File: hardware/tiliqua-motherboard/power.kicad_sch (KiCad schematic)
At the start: 32 parts, among them J6 CONN 2x5 P=2.54mm, U10 TPS7A91, U5 AP63200WU

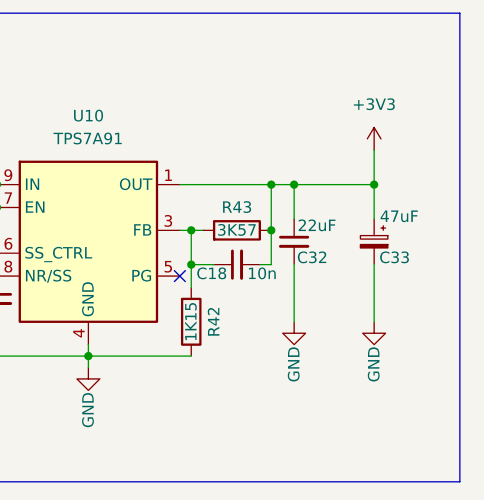
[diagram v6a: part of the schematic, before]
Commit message: hw/mobo-r3: 2nd electrolytic, OSHW on top, layout cleanup
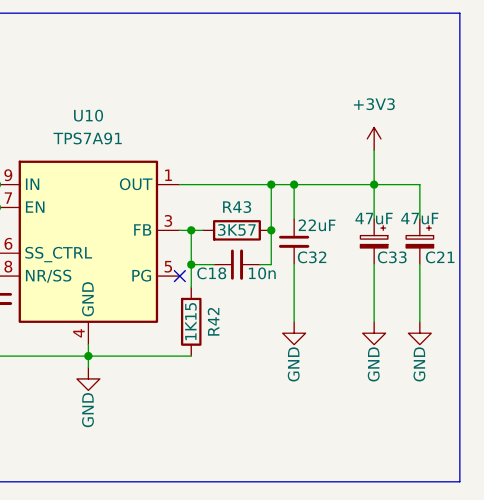
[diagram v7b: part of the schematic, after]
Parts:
- added C21: 47uF, Capacitor_SMD:CP_Elec_6.3x5.4, symbol Device:C_Polarized_Small
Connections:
- net +3V3: now also C21.1
- net GND: now also C21.2
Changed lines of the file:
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@@
 	(wire
 		(pts
+			(xy 274.32 118.11) (xy 274.32 114.3)
+		)
+		(stroke
+			(width 0)
+			(type default)
+		)
+	)
+	(wire
+		(pts
 			(xy 50.8 111.76) (xy 58.42 111.76)
 		)
@@
 	(wire
 		(pts
+			(xy 274.32 123.19) (xy 274.32 129.54)
+		)
+		(stroke
+			(width 0)
+			(type default)
+		)
+	)
+	(wire
+		(pts
 			(xy 237.49 133.35) (xy 237.49 132.08)
 		)
@@
 	(wire
 		(pts
+			(xy 274.32 114.3) (xy 269.24 114.3)
+		)
+		(stroke
+			(width 0)
+			(type default)
+		)
+	)
+	(wire
+		(pts
 			(xy 139.7 123.19) (xy 139.7 129.54)
 		)
@@
 	)
 	(symbol
+		(lib_id "power:GND")
+		(at 274.32 129.54 0)
+		(mirror y)
+		(unit 1)
+		(exclude_from_sim no)
+		(in_bom yes)
+		(on_board yes)
+		(dnp no)
+		(property "Reference" "#PWR012"
+			(at 274.32 135.89 0)
+			(effects
+				(font
+					(size 1.27 1.27)
+				)
+				(hide yes)
+			)
+		)
+		(property "Value" "GND"
+			(at 274.32 136.271 90)
+			(effects
+				(font
+					(size 1.27 1.27)
+				)
+				(justify left)
+			)
+		)
+		(property "Footprint" ""
+			(at 274.32 129.54 0)
+			(effects
+				(font
+					(size 1.27 1.27)
+				)
+				(hide yes)
+			)
+		)
+		(property "Datasheet" ""
+			(at 274.32 129.54 0)
+			(effects
+				(font
+					(size 1.27 1.27)
+				)
+				(hide yes)
+			)
+		)
+		(property "Description" ""
+			(at 274.32 129.54 0)
+			(effects
+				(font
+					(size 1.27 1.27)
+				)
+				(hide yes)
+			)
+		)
+		(pin "1"
+		)
+		(instances
+			(project "tiliqua-motherboard"
+				(path "/df6062c3-a570-4505-924c-c7fe32df3670/4885642e-e1b2-4a9c-a477-910295b2621e"
+					(reference "#PWR012")
+					(unit 1)
+				)
+			)
+		)
+	)
+	(symbol
 		(lib_id "Device:L_Ferrite_Small")
 		(at 77.47 57.15 90)
@@
 	)
 	(symbol
+		(lib_id "Device:C_Polarized_Small")
+		(at 274.32 120.65 0)
+		(mirror y)
+		(unit 1)
+		(exclude_from_sim no)
+		(in_bom yes)
+		(on_board yes)
+		(dnp no)
+		(property "Reference" "C21"
+			(at 276.606 122.428 0)
+			(effects
+				(font
+					(size 1.27 1.27)
+				)
+			)
+		)
+		(property "Value" "47uF"
+			(at 274.32 118.11 0)
+			(effects
+				(font
+					(size 1.27 1.27)
+				)
+			)
+		)
+		(property "Footprint" "Capacitor_SMD:CP_Elec_6.3x5.4"
+			(at 274.32 120.65 0)
+			(effects
+				(font
+					(size 1.27 1.27)
+				)
+				(hide yes)
+			)
+		)
+		(property "Datasheet" "https://datasheet.lcsc.com/lcsc/1809050343_Rubycon-25SEV47M6-3X5-5_C88735.pdf"
+			(at 274.32 120.65 0)
+			(effects
+				(font
+					(size 1.27 1.27)
+				)
+				(hide yes)
+			)
+		)
+		(property "Description" ""
+			(at 274.32 120.65 0)
+			(effects
+				(font
+					(size 1.27 1.27)
+				)
+				(hide yes)
+			)
+		)
+		(property "dig#" ""
+			(at 271.78 128.27 0)
+			(effects
+				(font
+					(size 1.27 1.27)
+				)
+				(hide yes)
+			)
+		)
+		(property "mfg#" "25SEV47M6.3X5.5"
+			(at 271.78 130.81 0)
+			(effects
+				(font
+					(size 1.27 1.27)
+				)
+				(hide yes)
+			)
+		)
+		(property "lcsc#" "C88735"
+			(at 274.32 120.65 0)
+			(effects
+				(font
+					(size 1.27 1.27)
+				)
+				(hide yes)
+			)
+		)
+		(property "Tol" ""
+			(at 274.32 120.65 0)
+			(effects
+				(font
+					(size 1.27 1.27)
+				)
+				(hide yes)
+			)
+		)
+		(pin "1"
+		)
+		(pin "2"
+		)
+		(instances
+			(project "tiliqua-motherboard"
+				(path "/df6062c3-a570-4505-924c-c7fe32df3670/4885642e-e1b2-4a9c-a477-910295b2621e"
+					(reference "C21")
+					(unit 1)
+				)
+			)
+		)
+	)
+	(symbol
 		(lib_id "Diode:US1G")
 		(at 66.04 58.42 0)
@@
 		(dnp no)
 		(property "Reference" "C33"
-			(at 271.526 122.428 0)
+			(at 271.272 122.428 0)
 			(effects
 				(font
@@
 		)
 		(property "Value" "47uF"
-			(at 272.034 117.856 0)
+			(at 269.24 118.11 0)
 			(effects
 				(font

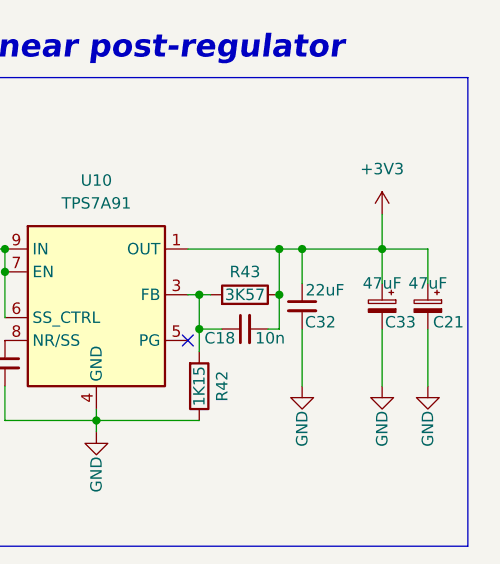
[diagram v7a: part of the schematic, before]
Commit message: hw/mobo-r3: assign remaining part numbers
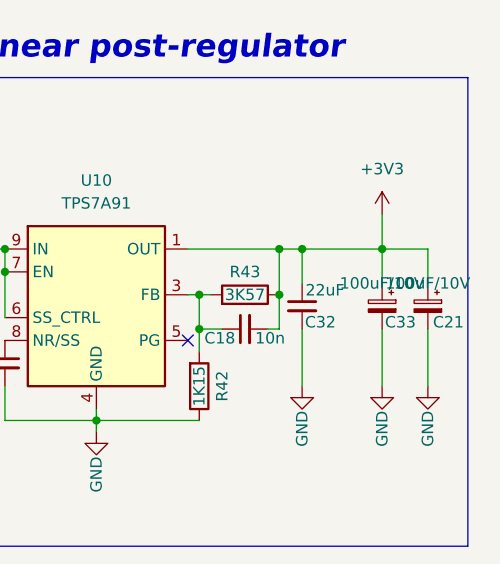
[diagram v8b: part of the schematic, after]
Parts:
- C17, C25, C28, C30: lcsc# (none) -> C131394
- C21, C33: value 47uF -> 100uF/10V; lcsc# C88735 -> C88795
- C31: lcsc# (none) -> C77177
- R42: lcsc# (none) -> C29401
- R43: lcsc# (none) -> C270609
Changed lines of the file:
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@@
 			)
 		)
-		(property "lcsc#" ""
+		(property "lcsc#" "C131394"
 			(at 50.8 115.57 0)
 			(effects
@@
 			)
 		)
-		(property "Value" "47uF"
+		(property "Value" "100uF/10V"
 			(at 274.32 118.11 0)
 			(effects
@@
 			)
 		)
-		(property "lcsc#" "C88735"
+		(property "lcsc#" "C88795"
 			(at 274.32 120.65 0)
 			(effects
@@
 			)
 		)
-		(property "lcsc#" ""
+		(property "lcsc#" "C131394"
 			(at 227.33 127 0)
 			(effects
@@
 			)
 		)
-		(property "lcsc#" ""
+		(property "lcsc#" "C131394"
 			(at 215.9 120.65 0)
 			(effects
@@
 			)
 		)
-		(property "lcsc#" ""
+		(property "lcsc#" "C131394"
 			(at 88.9 114.3 0)
 			(effects
@@
 			)
 		)
-		(property "Value" "47uF"
+		(property "Value" "100uF/10V"
 			(at 269.24 118.11 0)
 			(effects
@@
 			)
 		)
-		(property "lcsc#" "C88735"
+		(property "lcsc#" "C88795"
 			(at 269.24 120.65 0)
 			(effects
@@
 			)
 		)
-		(property "lcsc#" ""
+		(property "lcsc#" "C77177"
 			(at 109.22 118.11 0)
 			(effects
@@
 			)
 		)
-		(property "lcsc#" ""
+		(property "lcsc#" "C270609"
 			(at 254 119.38 0)
 			(effects
@@
 			)
 		)
-		(property "lcsc#" ""
+		(property "lcsc#" "C29401"
 			(at 248.92 129.54 0)
 			(effects
